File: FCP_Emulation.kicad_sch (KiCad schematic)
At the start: 94 parts, among them J1 Conn_01x10_Female, J2 Conn_01x10_Female, J3 Conn_01x10_Female, J4 Conn_01x02_Female, J5 Conn_01x02_Female, U1 LM2902, U2 LM2902, U3 LM2902, U4 LM324, U5 LM324, U6 LM324, U7 LM2902, U9 LM324

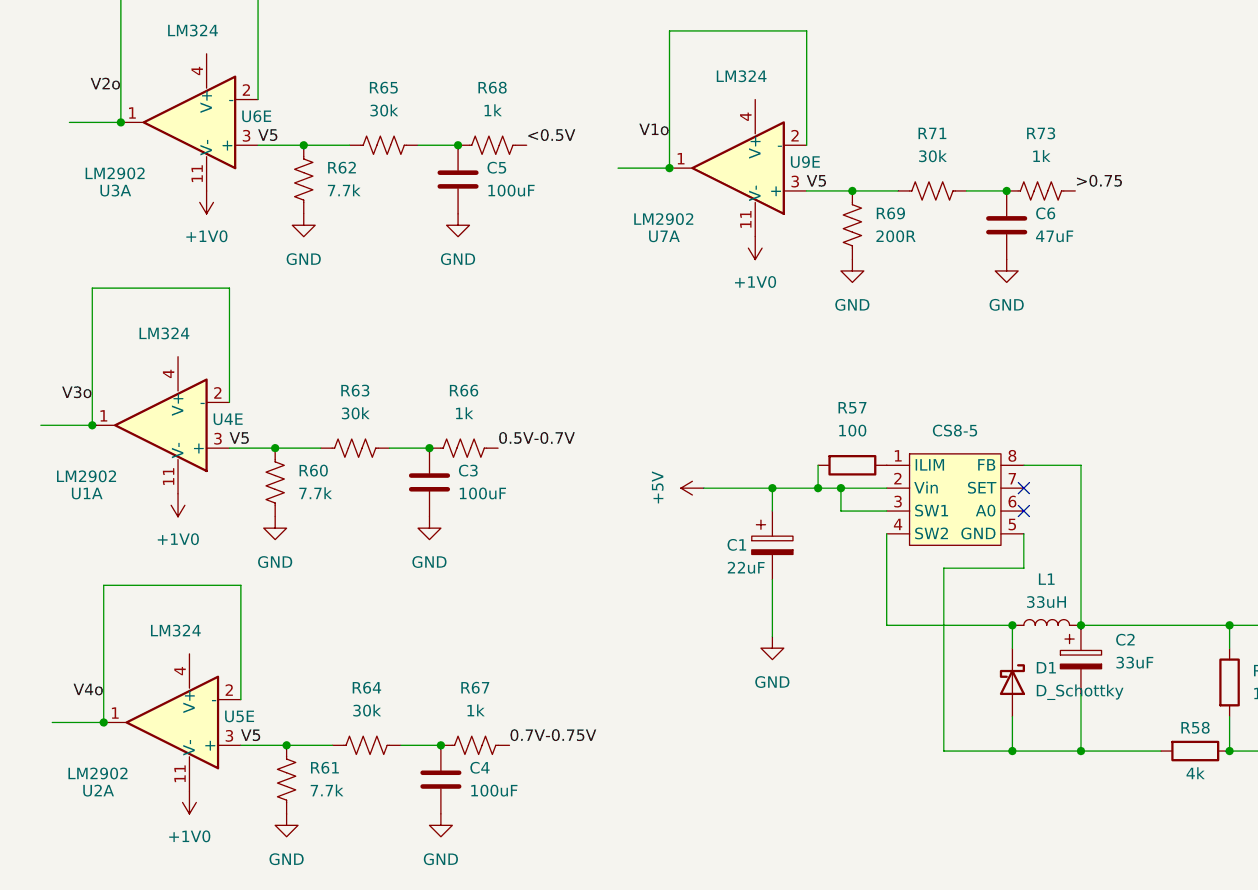
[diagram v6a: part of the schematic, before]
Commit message: positive case specced
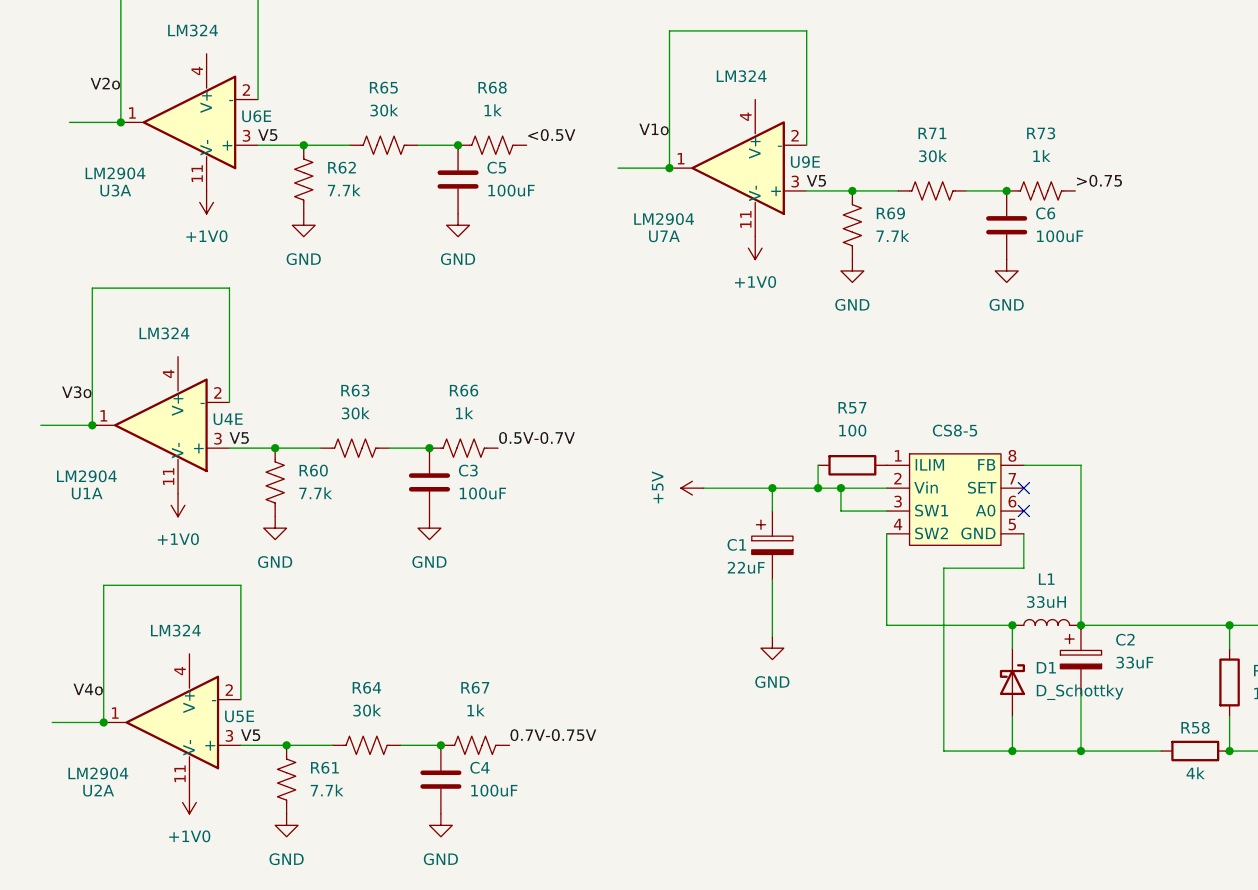
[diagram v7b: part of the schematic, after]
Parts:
- C3, C4, C5: footprint (none) -> Capacitor_SMD:C_0805_2012Metric
- C6: value 47uF -> 100uF; footprint (none) -> Capacitor_SMD:C_0805_2012Metric
- R60, R61, R62, R63, R64, R65, R66, R67, R68, R71, R73: footprint (none) -> Resistor_SMD:R_0603_1608Metric
- R69: value 200R -> 7.7k; footprint (none) -> Resistor_SMD:R_0603_1608Metric
- U1, U2, U3, U7: value LM2902 -> LM2904; footprint Package_SO:SO-14_3.9x8.65mm_P1.27mm -> Package_SO:SOIC-8-N7_3.9x4.9mm_P1.27mm

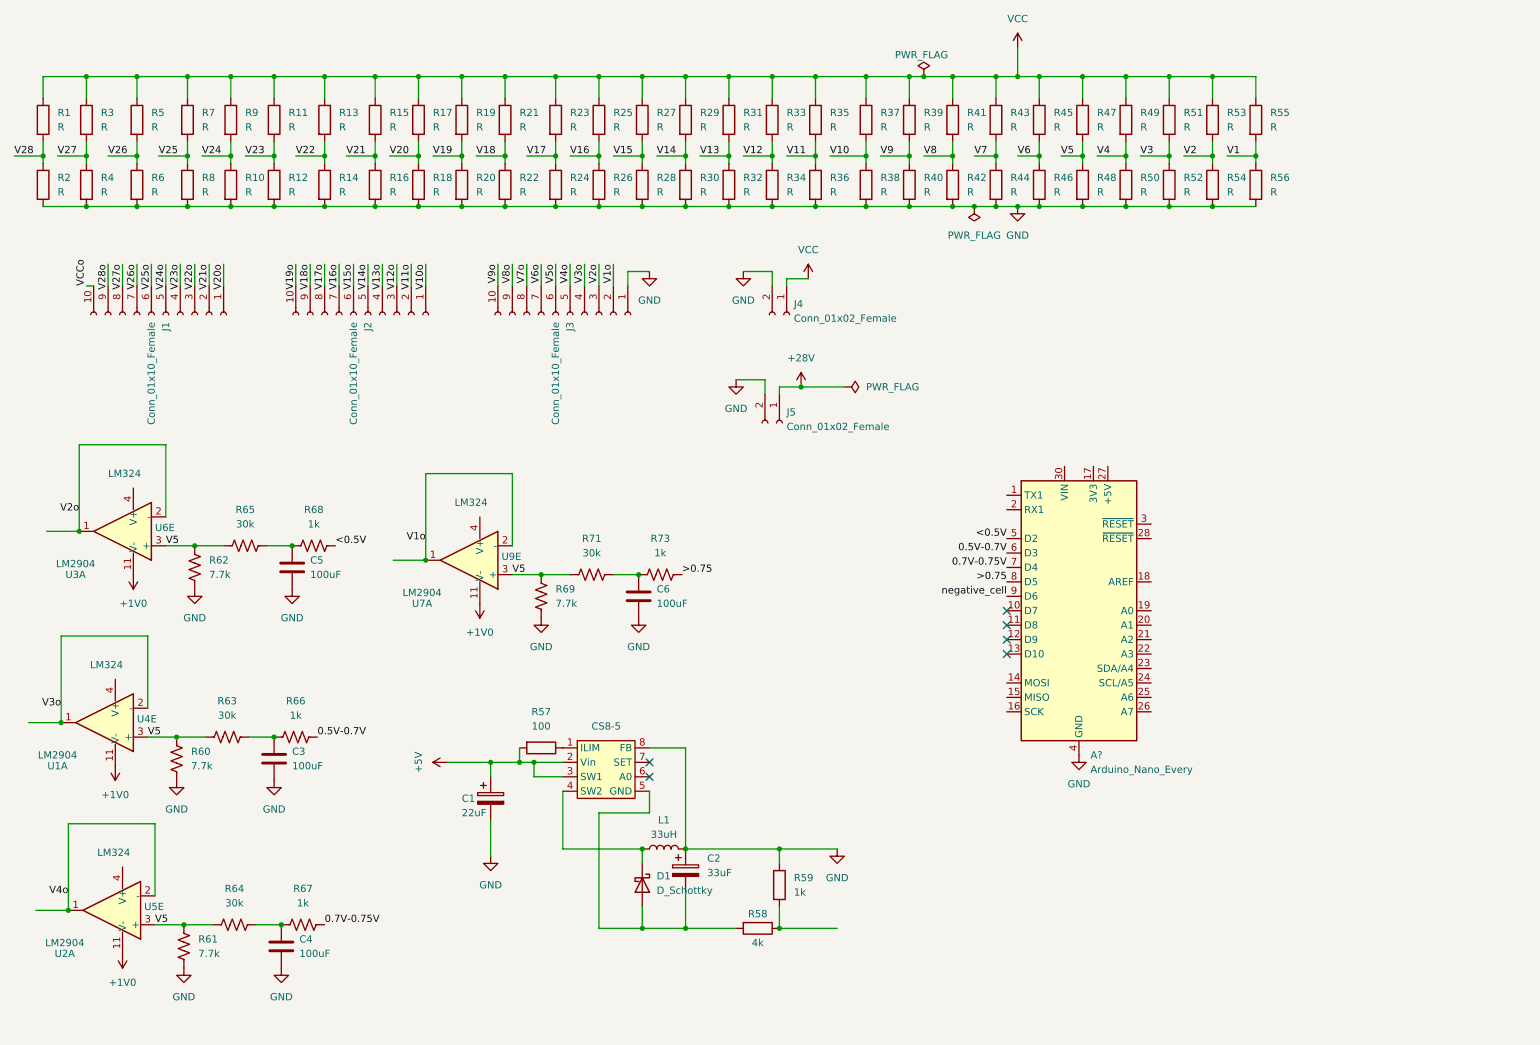
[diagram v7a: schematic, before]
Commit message: fixed some ERC errors
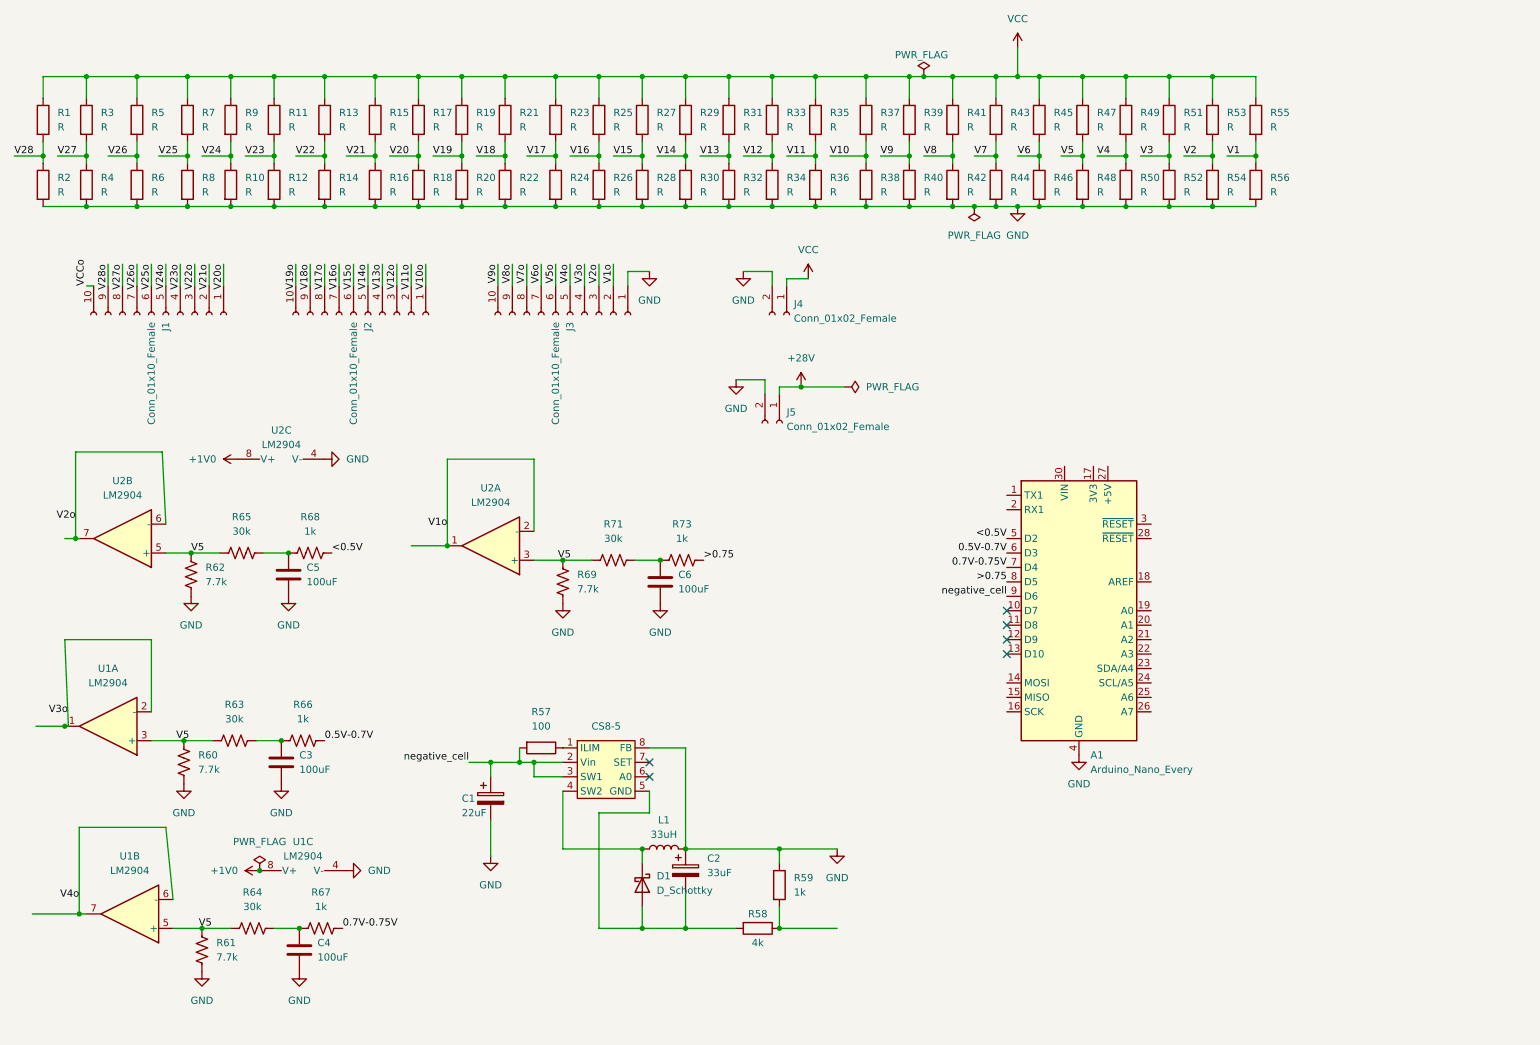
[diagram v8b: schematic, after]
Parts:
- removed U1, U2, U3, U7: LM2904, Package_SO:SOIC-8-N7_3.9x4.9mm_P1.27mm, symbol Amplifier_Operational:LM2902
- removed U4, U5, U6, U9: LM324, symbol Amplifier_Operational:LM324
- added U1, U2: LM2904, Package_SO:SOIC-8-N7_3.9x4.9mm_P1.27mm, symbol Amplifier_Operational:LM2904
- gave numbers to parts that had none: 1
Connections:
- net +5V is gone; now on net negative_cell: C1.1, CS8-5.2 (Vin), CS8-5.3 (SW1), R57.2
- net +1V0: now also U1.8 (V+), U2.8 (V+)
- net GND: now also U1.4 (V-), U2.4 (V-)
- net V1o: now also U2.1, U2.2 (-)
- net V2o: now also U2.6 (-), U2.7
- net V3o: now also U1.1, U1.2 (-)
- net V4o: now also U1.6 (-), U1.7
- net V5: now also U1.3 (+), U1.5 (+), U2.3 (+), U2.5 (+)
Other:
- moved on the sheet: C3, C4, C5, C6, R60, R61, R62, R63, R64, R65, R66, R67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
